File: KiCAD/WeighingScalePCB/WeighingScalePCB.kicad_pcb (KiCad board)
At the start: 4 copper layers, 94.6 x 73.3 mm, 37 parts, among them J1 Conn_01x04_Pin, U10 LMC555xMM, U2 HX711, U3 LMC555xMM

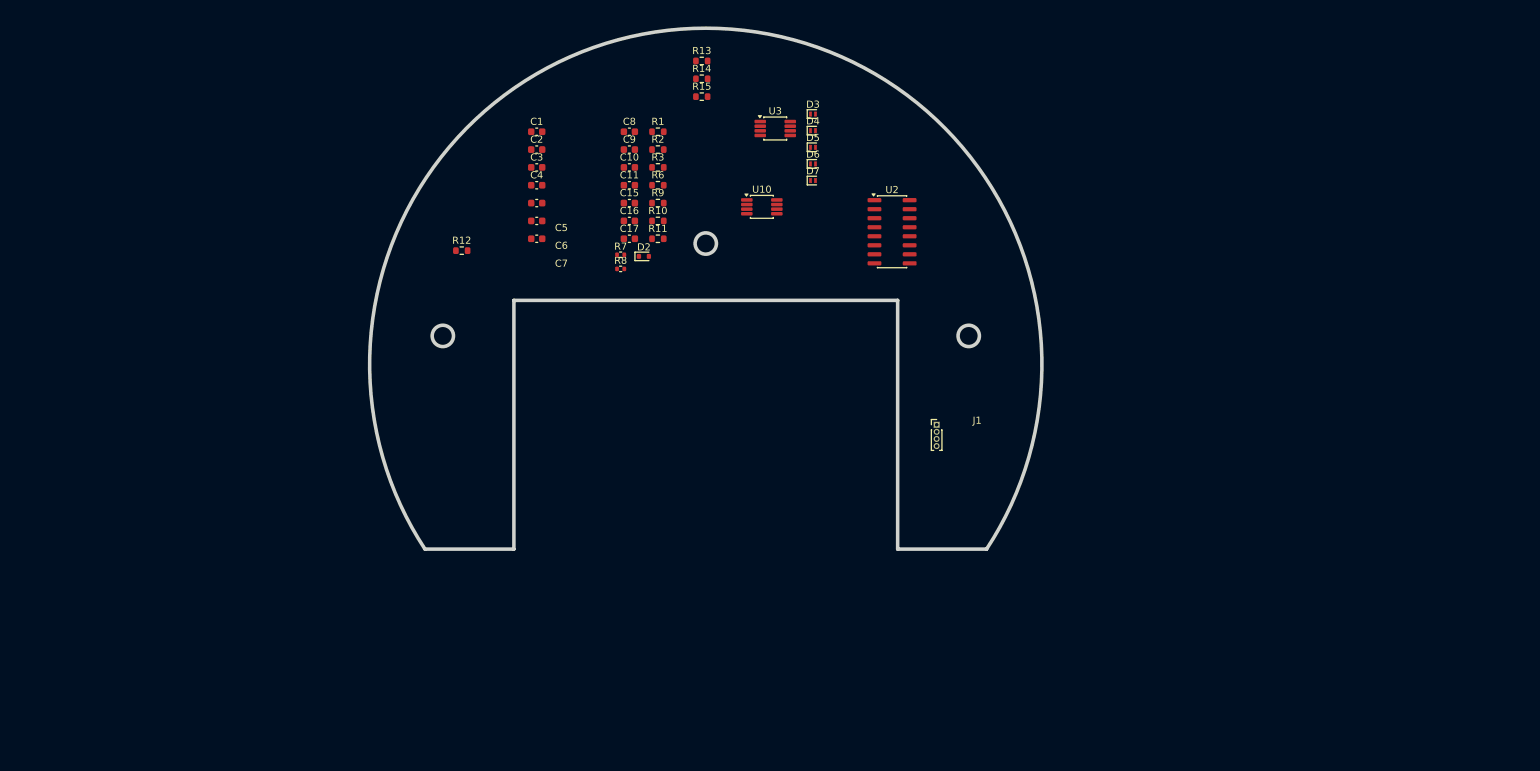
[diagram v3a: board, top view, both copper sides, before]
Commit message: assigned footprints
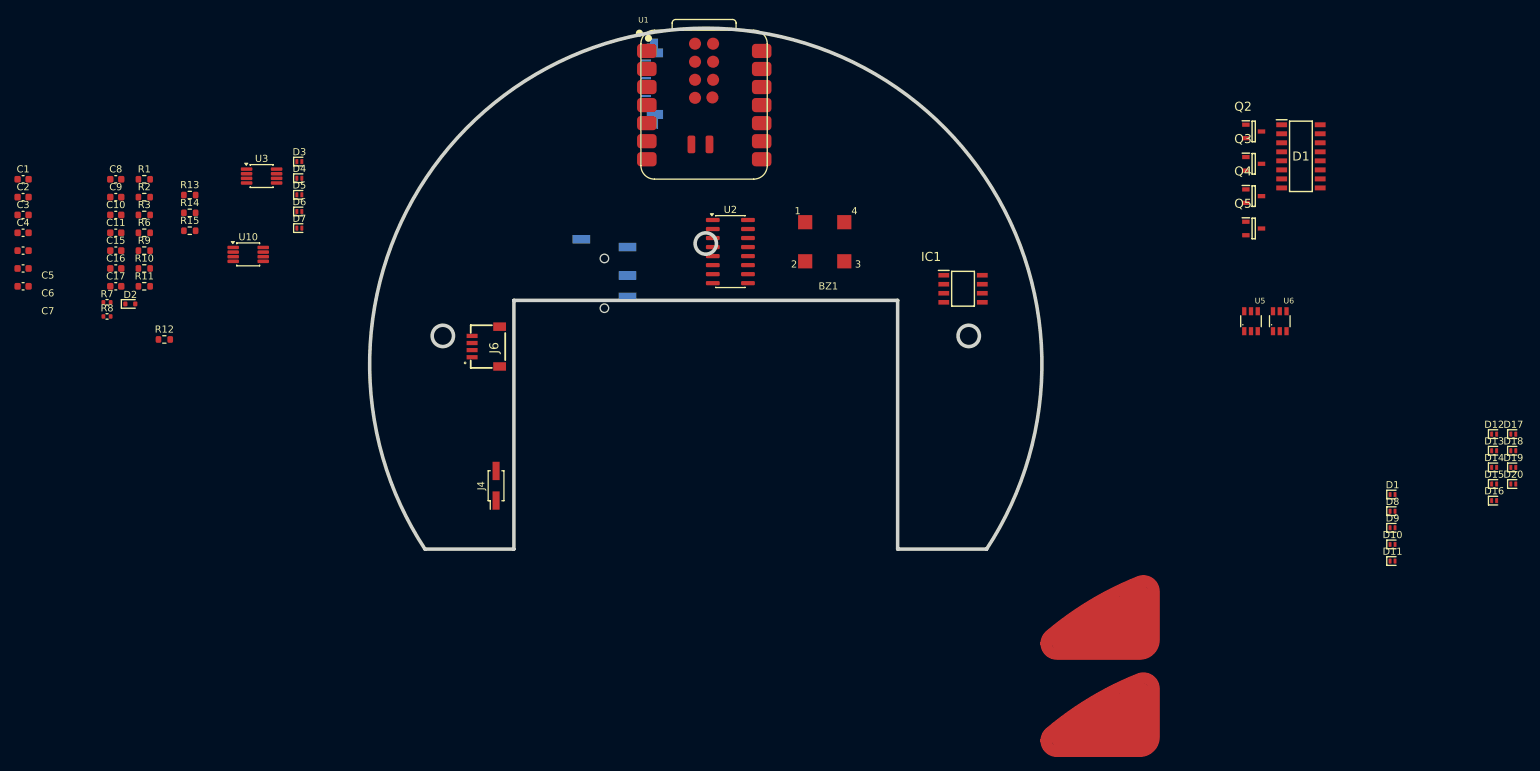
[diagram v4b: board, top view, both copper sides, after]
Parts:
- added BZ1: Buzzer, Footprints:CL7525A_buzzer, F.Cu at (164.2, 76.0)
- added D1: SP720ABTG, KiCad:SOIC127P600X175-16N, F.Cu at (230.8, 54.7)
- added D1: PESD3V3U1UL, Diode_SMD:D_SOD-882, F.Cu at (243.7, 102.3)
- added D10: PESD3V3U1UL, Diode_SMD:D_SOD-882, F.Cu at (243.7, 109.3)
- added D11: PESD3V3U1UL, Diode_SMD:D_SOD-882, F.Cu at (243.7, 111.7)
- added D12: PESD3V3U1UL, Diode_SMD:D_SOD-882, F.Cu at (258.0, 93.8)
- added D13: PESD3V3U1UL, Diode_SMD:D_SOD-882, F.Cu at (258.0, 96.2)
- added D14: PESD3V3U1UL, Diode_SMD:D_SOD-882, F.Cu at (258.0, 98.5)
- added D15: PESD3V3U1UL, Diode_SMD:D_SOD-882, F.Cu at (258.0, 100.8)
- added D16: PESD3V3U1UL, Diode_SMD:D_SOD-882, F.Cu at (258.0, 103.2)
- added D17: PESD3V3U1UL, Diode_SMD:D_SOD-882, F.Cu at (260.6, 93.8)
- added D18: PESD3V3U1UL, Diode_SMD:D_SOD-882, F.Cu at (260.6, 96.2)
- added D19: PESD3V3U1UL, Diode_SMD:D_SOD-882, F.Cu at (260.6, 98.5)
- added D20: PESD3V3U1UL, Diode_SMD:D_SOD-882, F.Cu at (260.6, 100.8)
- added D8: PESD3V3U1UL, Diode_SMD:D_SOD-882, F.Cu at (243.7, 104.7)
- added D9: PESD3V3U1UL, Diode_SMD:D_SOD-882, F.Cu at (243.7, 107.0)
- added IC1: MAX6675ISA+T, Footprints:SOIC127P600X175-8N_MAX6675, F.Cu at (183.2, 73.4)
- added J2: AudioJack4, Footprints:PRT12639_thermocouple_conn, B.Cu at (132.8, 72.7)
- added J4: Battery Conn, Connector_PinHeader_2.00mm:PinHeader_2x01_P2.00mm_Vertical_SMD, F.Cu at (117.5, 101.1)
- added J6: Conn_01x04_MountingPin, Footprints:SM04B-SRSS-TB_LFSN_, F.Cu at (118.8, 84.5)
- added Q2: NX138AKR, Footprints:SOT95P230X110-3N, F.Cu at (224.1, 51.2)
- added Q3: NX138AKR, Footprints:SOT95P230X110-3N, F.Cu at (224.1, 55.8)
- added Q4: NX138AKR, Footprints:SOT95P230X110-3N, F.Cu at (224.1, 60.3)
- added Q5: NX138AKR, Footprints:SOT95P230X110-3N, F.Cu at (224.1, 64.9)
- added T1: TouchPad, Footprints:touchpad, F.Cu at (202.1, 126.1)
- added T2: TouchPad, Footprints:touchpad, F.Cu at (202.1, 139.8)
- added U1: XIAO-ESP32-S3-SMD, Footprints:XIAO-ESP32C6-SMD (1), F.Cu at (147.0, 47.5)
- added U5: TTP223-BA6, Footprints:SOT23-6_touchpad_sensor, F.Cu at (223.7, 77.9)
- added U6: TTP223-BA6, Footprints:SOT23-6_touchpad_sensor, F.Cu at (227.8, 77.9)
- J1: value Conn_01x04_Pin -> Conn_01x14_MountingPin; footprint Connector_PinHeader_1.00mm:PinHeader_1x04_P1.00mm_Vertical -> Footprints:SFV14R3STBE1HLF_oled_conn; moved to B.Cu
- R11: value 200K -> 5K
- moved R15 74.5 mm to (74.4, 65.2)
- moved R13 74.5 mm to (74.4, 60.2)
- moved R14 74.5 mm to (74.4, 62.7)
- moved D2 72.6 mm to (66.0, 75.5)
- moved R1 72.6 mm to (68.0, 58.0)
- moved R10 72.6 mm to (68.0, 70.5)
- moved R11 72.6 mm to (68.0, 73.0)
- moved R2 72.6 mm to (68.0, 60.5)
- moved R3 72.6 mm to (68.0, 63.0)
- moved R6 72.6 mm to (68.0, 65.5)
- moved R7 72.6 mm to (62.8, 75.3)
- moved R8 72.6 mm to (62.8, 77.3)
- moved R9 72.6 mm to (68.0, 68.0)
- moved U10 72.6 mm to (82.6, 68.5)
- moved C1 72.6 mm to (51.0, 58.0)
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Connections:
- C3 pad 2: Net-(J1-Pin_1) -> Net-(J6-Pin_1)
- C4 pad 2: Net-(J1-Pin_1) -> Net-(J6-Pin_1)
- D2 pad 1: Net-(D2-K) -> Time
- J1 pad 1: Net-(J1-Pin_1) -> Net-(D20-K)
- J1 pad 2: GND -> Net-(D19-K)
- J1 pad 3: Net-(J1-Pin_3) -> Net-(D18-K)
- J1 pad 4: GND -> Net-(D17-K)
- R2 pad 1: Net-(J1-Pin_3) -> Net-(J6-Pin_3)
- U2 pad 3: Net-(J1-Pin_1) -> Net-(J6-Pin_1)

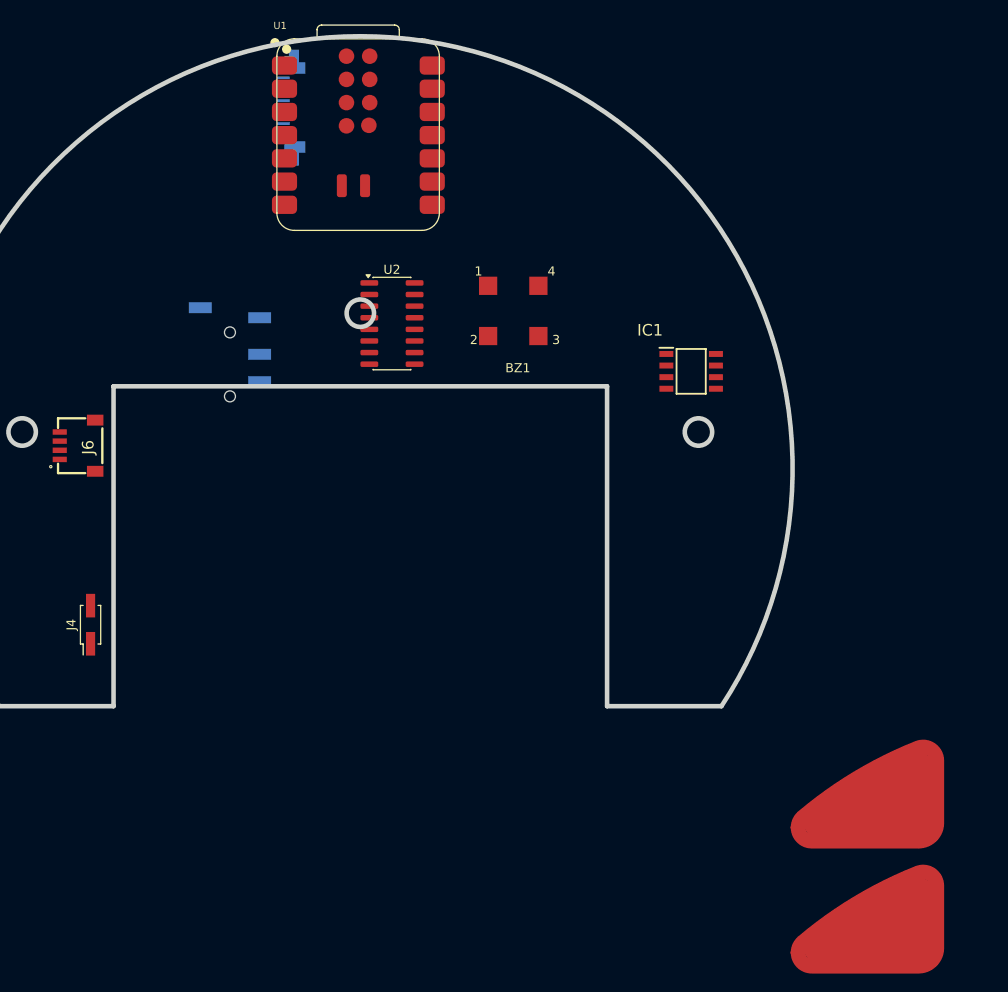
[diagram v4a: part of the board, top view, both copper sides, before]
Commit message: added toucpad and all fps, only ferrite selection pending
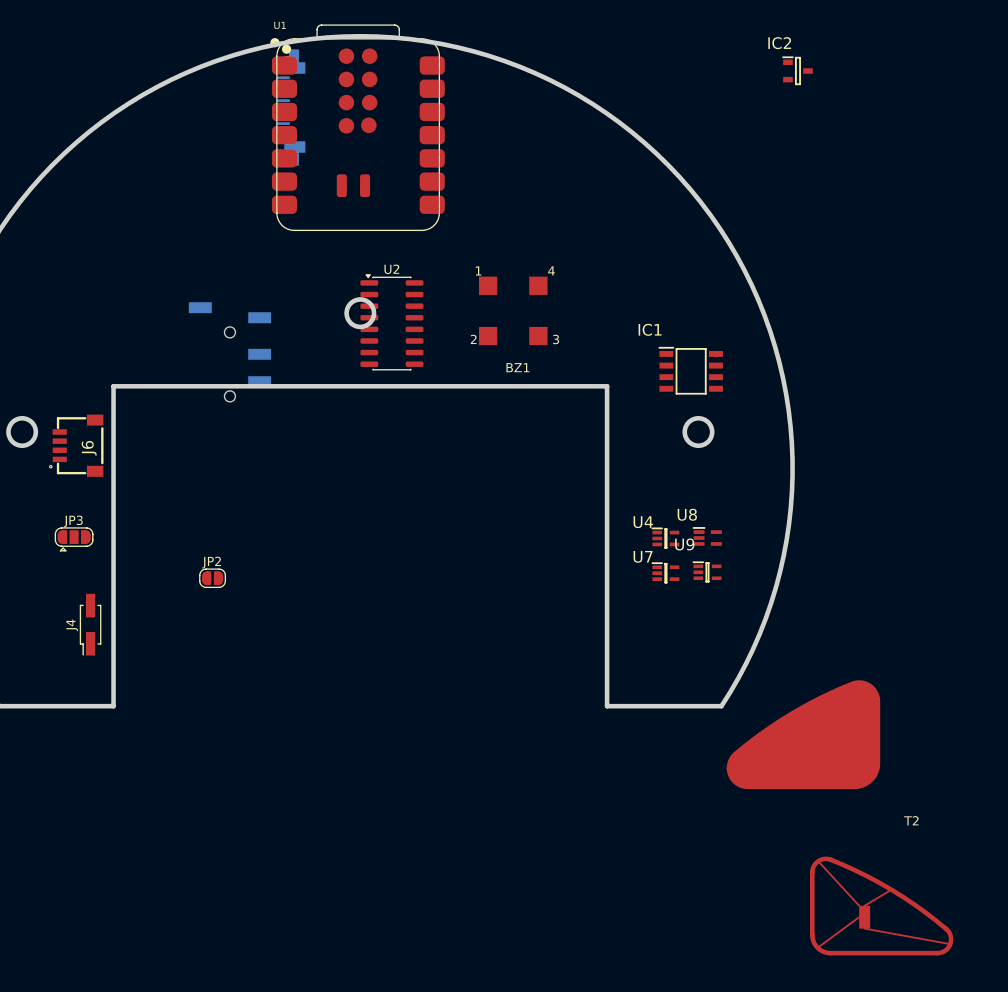
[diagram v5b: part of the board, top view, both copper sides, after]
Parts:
- added IC2: APS11753KMDALX-9PL5, Footprints:SOT95P240X115-3N_Hall effect, F.Cu at (194.9, 40.5)
- added JP2: SolderJumper_2_Open, Jumper:SolderJumper-2_P1.3mm_Open_RoundedPad1.0x1.5mm, F.Cu at (130.8, 96.0)
- added JP3: rate setting, Jumper:SolderJumper-3_P1.3mm_Open_RoundedPad1.0x1.5mm, F.Cu at (115.7, 91.5)
- added U4: 74LVC1G79GW-Q100H, Footprints:SOT65P212X110-5N_D_FF, F.Cu at (180.4, 91.7)
- added U7: 74LVC1G79GW-Q100H, Footprints:SOT65P212X110-5N_D_FF, F.Cu at (180.4, 95.5)
- added U8: 74LVC1G04, Footprints:SOT65P210X110-5N_NOT, F.Cu at (185.0, 91.6)
- added U9: 74LVC1G08, Footprints:SOT65P212X110-5N_AND, F.Cu at (185.0, 95.3)
- T2: footprint Footprints:touchpad -> Footprints:touchpad 2
- moved T1 9.55 mm to (195.1, 119.6)
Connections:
- J1 pad 15: (no net) -> GND
- J1 pad 16: (no net) -> GND
- J2 pad 1: (no net) -> Net-(D6-K)
- J2 pad 2: (no net) -> Net-(D7-K)
- J2 pad 3: (no net) -> Net-(D6-K)
- J2 pad 4: (no net) -> Net-(D7-K)
- J6 pad 5: (no net) -> unconnected-(J6-MountPin-Pad5)
- J6 pad 6: (no net) -> unconnected-(J6-MountPin-Pad6)

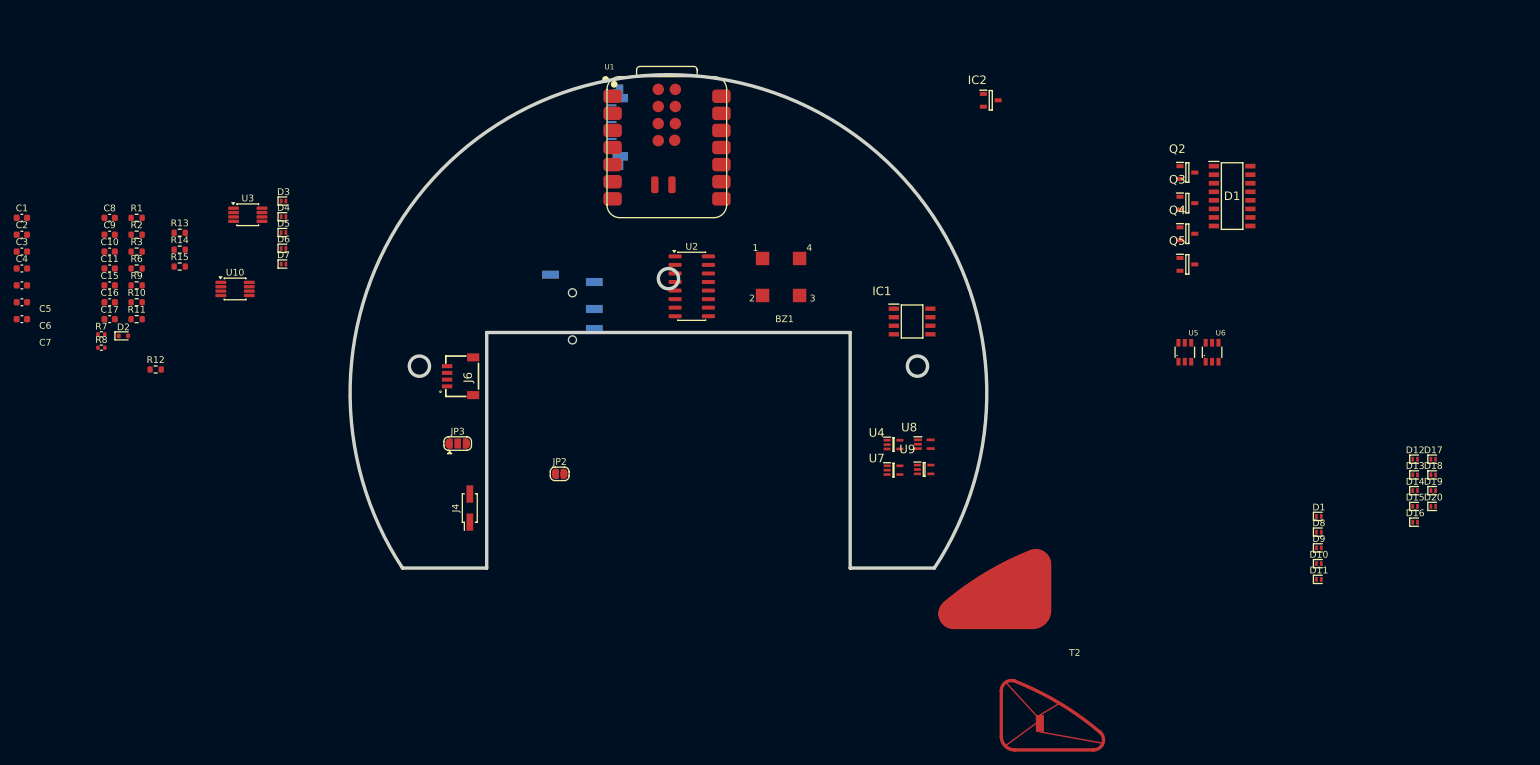
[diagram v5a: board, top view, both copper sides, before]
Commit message: added gnd plane fixed touch pad footprint, desiganed thermocouple amp, added ttp base ckt
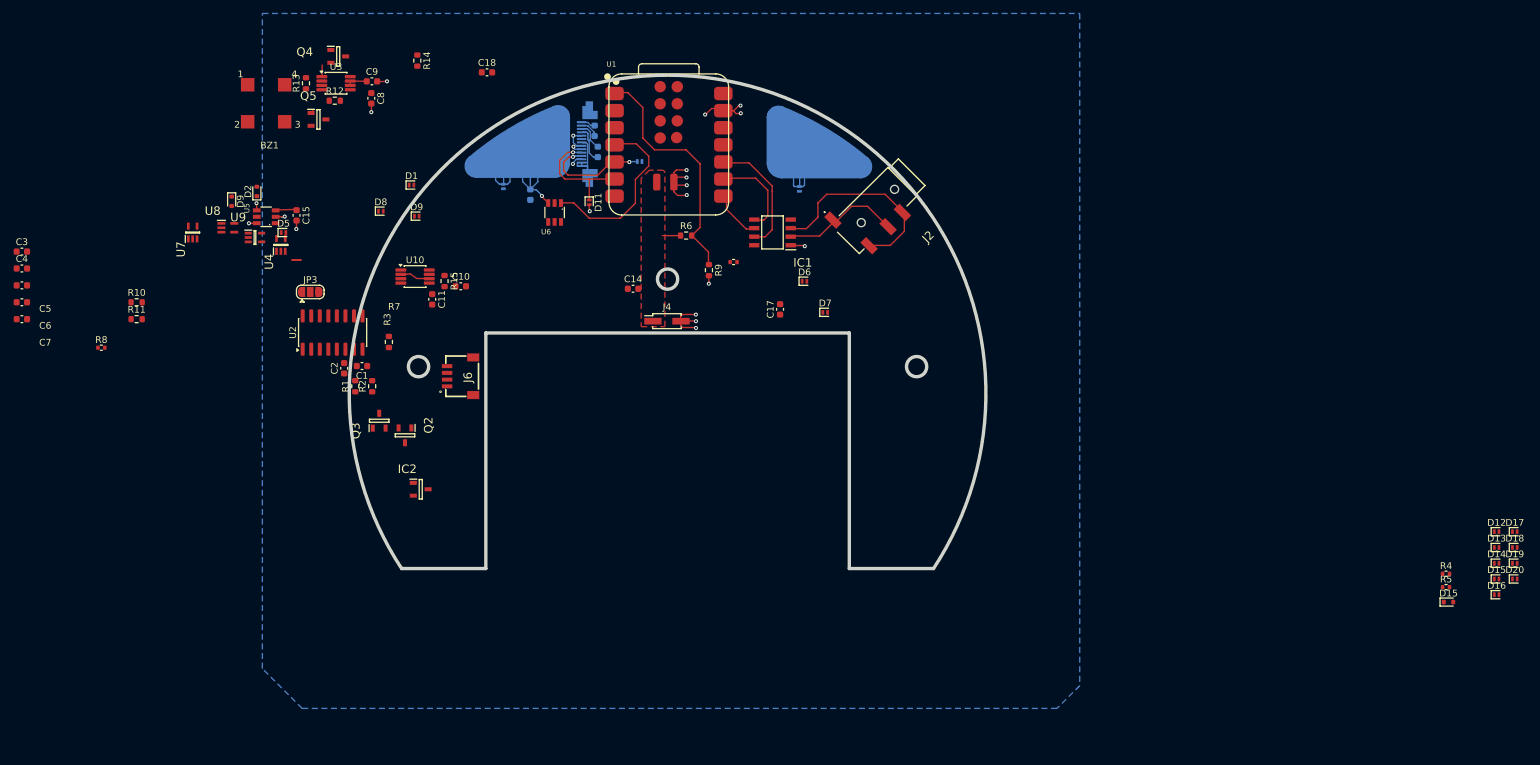
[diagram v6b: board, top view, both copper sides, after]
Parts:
- removed the D1 at (230.8, 54.7)
- removed JP2: SolderJumper_2_Open, Jumper:SolderJumper-2_P1.3mm_Open_RoundedPad1.0x1.5mm
- added C12: 1uF, Capacitor_SMD:C_0603_1608Metric, B.Cu at (136.0, 45.0)
- added C13: 1uF, Capacitor_SMD:C_0603_1608Metric, B.Cu at (136.5, 48.2)
- added C14: 1uF, Capacitor_SMD:C_0603_1608Metric, F.Cu at (141.8, 68.5)
- added C18: 1uF, Capacitor_SMD:C_0603_1608Metric, F.Cu at (120.1, 36.4)
- added D15: 1N4148WT, Diode_SMD:D_SOD-523, F.Cu at (262.9, 115.0)
- added D9: 1N4148WT, Diode_SMD:D_SOD-523, F.Cu at (82.1, 55.5)
- added R4: 10K, Resistor_SMD:R_0402_1005Metric, F.Cu at (262.5, 110.8)
- added R5: 330K, Resistor_SMD:R_0402_1005Metric, F.Cu at (262.5, 112.8)
- C16, D10, D3, D4: moved to B.Cu
- J2: moved to F.Cu
- moved D8 147.3 mm to (104.3, 57.0)
- moved D1 143.5 mm to (108.8, 53.1)
- moved D9 142.8 mm to (109.6, 57.7)
- moved U5 138.0 mm to (87.2, 57.8), turned to 90 degrees
- moved Q5 130.9 mm to (95.0, 43.3)
- moved Q4 128.9 mm to (98.0, 34.0)
- moved Q3 124.3 mm to (104.0, 88.1), turned to 90 degrees
- moved Q2 122.6 mm to (107.9, 90.3), turned to -90 degrees
- moved D11 122.0 mm to (135.2, 55.7), turned to -90 degrees
- moved D10 117.3 mm to (142.7, 49.6)
- moved T2 114.0 mm to (126.5, 54.5)
- moved U7 109.9 mm to (76.3, 60.1), turned to 90 degrees
- moved U8 108.4 mm to (81.5, 59.4)
- moved U9 105.2 mm to (85.6, 60.9)
- moved IC2 102.5 mm to (110.2, 98.3)
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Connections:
- net Net-(D12-K) renamed /d15
- net Net-(D17-K) renamed /c13_2
- net Net-(D18-K) renamed /c13_1
- net Net-(D19-K) renamed /c12_2
- net Net-(D20-K) renamed /c12_1
- net Net-(D4-K) renamed /touch2
- net Net-(D6-K) renamed /T+
- net Net-(D7-K) renamed /T-
- net Net-(J6-Pin_1) renamed /DVDD_ldcell
- C15 pad 1: Net-(D3-K) -> /touch1
- D10 pad 1: Net-(D10-K) -> SDA
- D11 pad 1: Net-(D11-K) -> SCL
- D13 pad 1: Net-(D13-K) -> VCC
- D16 pad 1: Net-(D16-K) -> VCC
- D2 pad 1: Time -> /timeORtare
- D3 pad 1: Net-(D3-K) -> /touch1
- J1 pad 10: Net-(D11-K) -> SCL
- J1 pad 11: Net-(D10-K) -> SDA
- J1 pad 12: Net-(D9-K) -> /R5
- J1 pad 13: Net-(D8-K) -> GND
- J1 pad 14: Net-(D1-K) -> GND
- J1 pad 5: Net-(D16-K) -> VCC
- J1 pad 6: Net-(D15-K) -> unconnected-(J1-Pin_6-Pad6)
- J1 pad 7: Net-(D14-K) -> GND
- J1 pad 8: Net-(D13-K) -> VCC
- J4 pad 2: Net-(J4-Pin_2) -> GND
- U1 pad 16: Net-(J4-Pin_2) -> GND
- U5 pad 3: Net-(D3-K) -> /touch1
- U7 pad 1: Time -> /timeORtare
- U9 pad 2: Time -> /timeORtare
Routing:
- net VCC: vias 0 -> 1
- net SDA: vias 0 -> 2
- net SCL: vias 0 -> 1
- net GND: vias 0 -> 19
- net /touch2: vias 0 -> 1
- net /d15: vias 0 -> 1
- net /R5: vias 0 -> 1
- added copper zone on F.Cu, net /V_BAT
- added copper zone on B.Cu, net GND
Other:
- copper layers 4 -> 2
- board text added: "${REFERENCE}"
